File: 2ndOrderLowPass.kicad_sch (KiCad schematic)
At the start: 14 parts, among them U2 LM2904DR, U3 LM2904DR

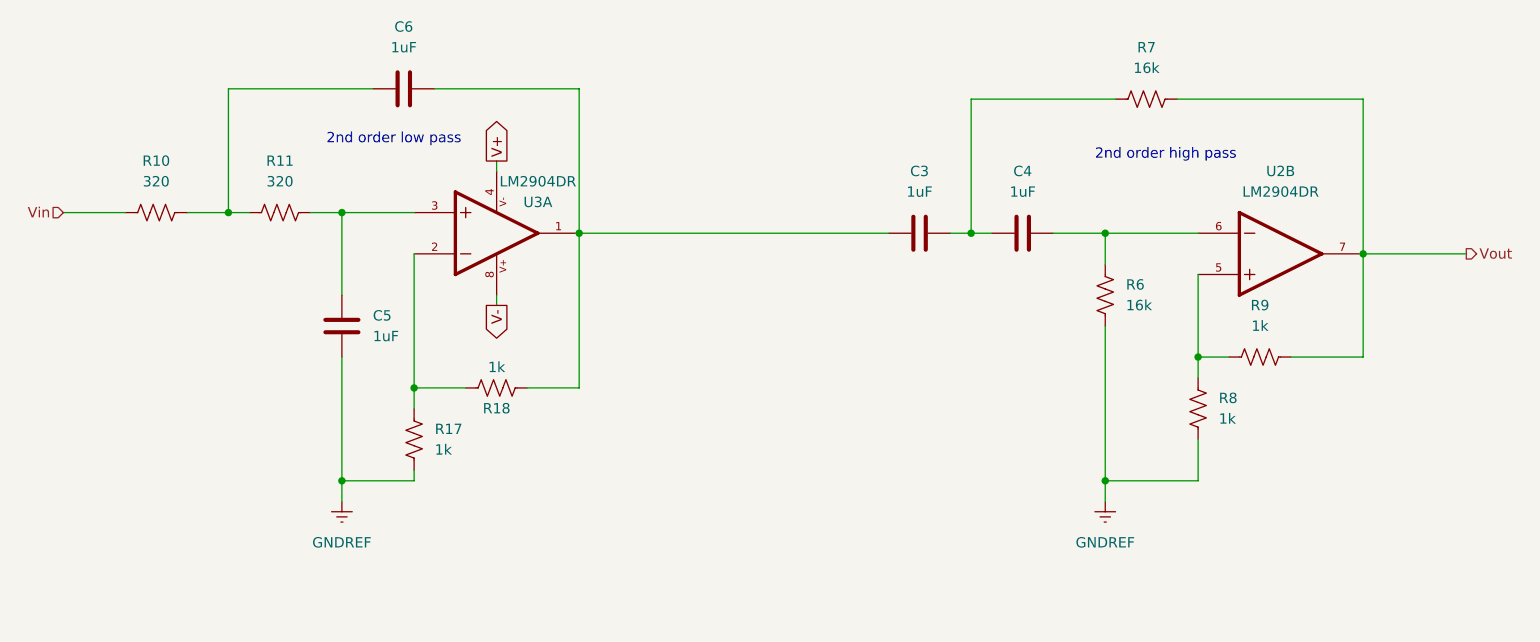
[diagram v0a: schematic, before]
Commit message: added new filter sims, and tweaked components for notch and bandpass filter and circuits for both as well
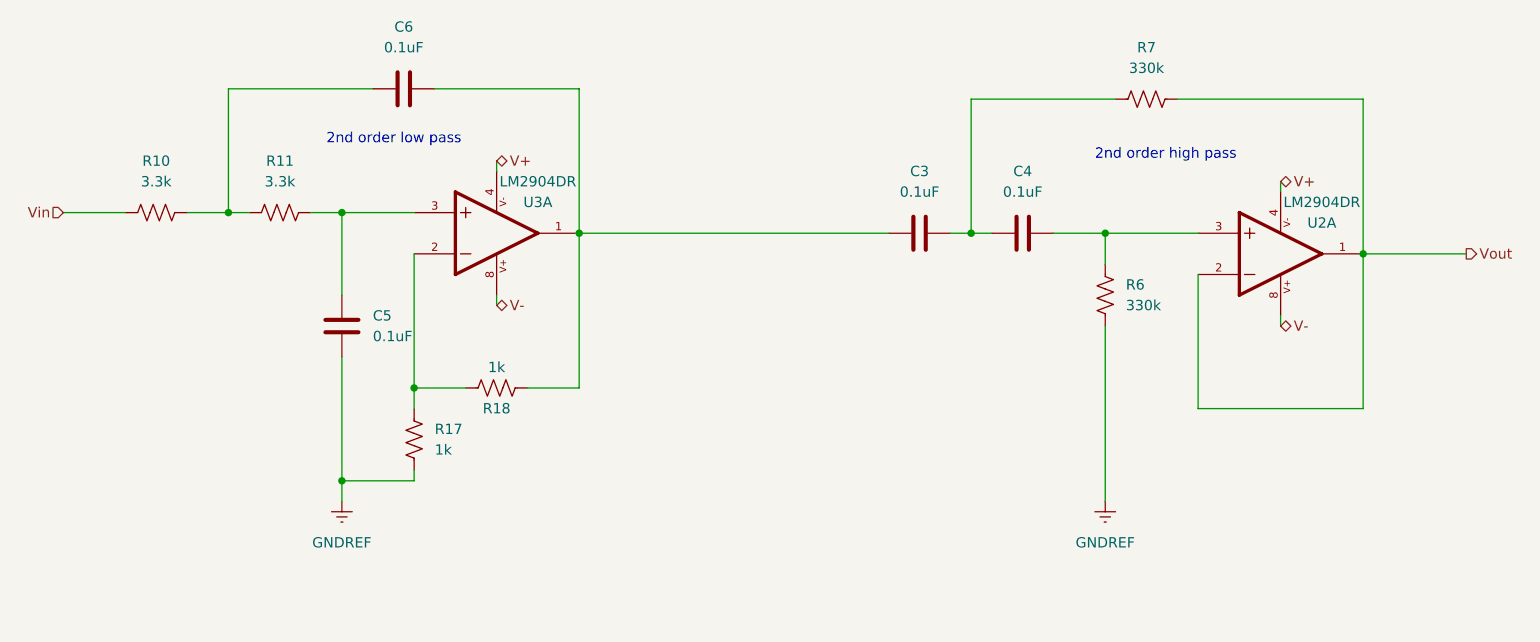
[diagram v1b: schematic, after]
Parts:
- removed R8, R9: 1k, symbol Device:R_US
- removed U2: LM2904DR, LM2904DR:SOIC127P599X175-8N, symbol Digikey2:LM2904DR
- added U2: LM2904DR, LM2904DR:SOIC127P599X175-8N, symbol Digikey2:LM2904DR
- C3, C4, C5, C6: value 1uF -> 0.1uF
- R10, R11: value 320 -> 3.3k
- R6, R7: value 16k -> 330k
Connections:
- net V+: now also U2.4
- net V-: now also U2.8
- net Vout: now also U2.1, U2.2
- net at C4.2, R6.1: now also U2.3

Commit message: swapped lpf and hpf in bandpass filter and added testpoints on various filter circuits
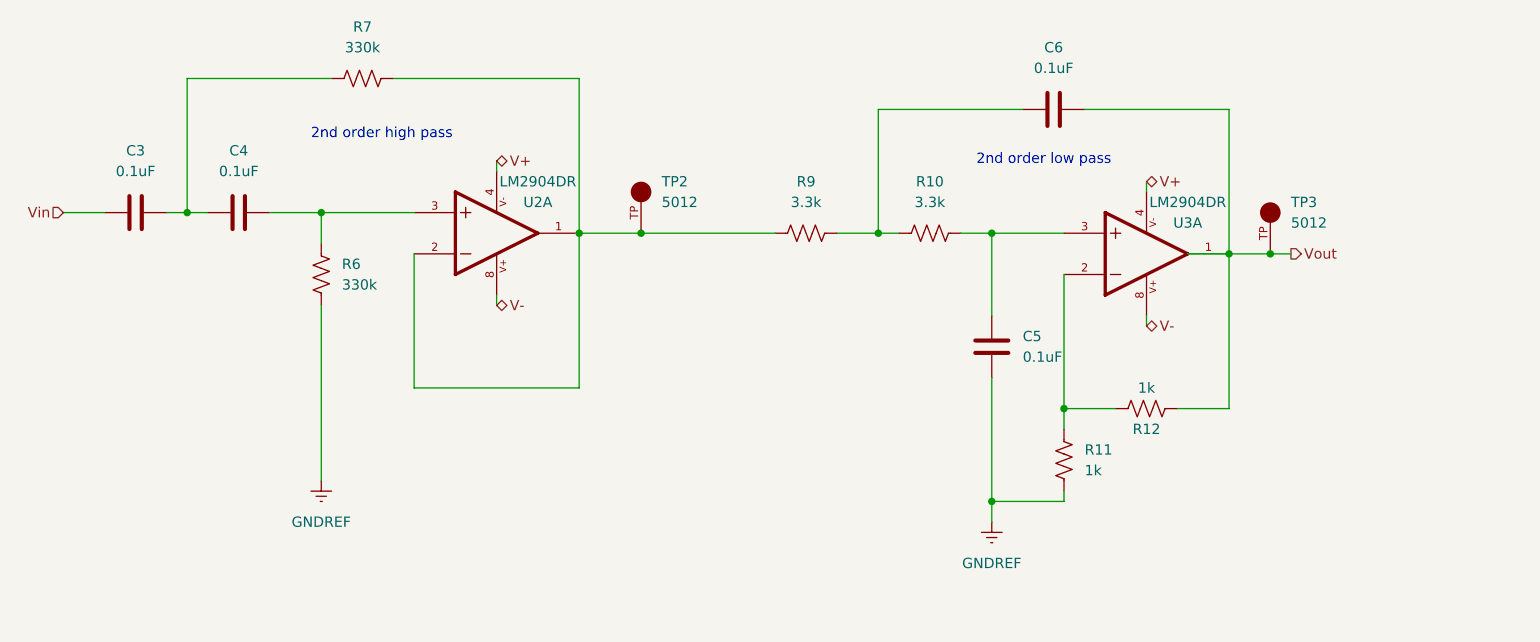
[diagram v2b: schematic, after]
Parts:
- removed R17, R18: 1k, symbol Device:R_US
- added R12: 1k, symbol Device:R_US
- added R9: 3.3k, symbol Device:R_US
- added TP2, TP3: 5012, 5012:TP_5012, symbol TP_5012:5012
- R11: value 3.3k -> 1k
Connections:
- net GNDREF: now also R11.2
- net Vin: now also C3.1; no longer R10.2
- net Vout: now also C6.2, U3.1, R12.2, TP3.TP; no longer R7.2, U2.1, U2.2
- net at U3.2: now also R11.1, R12.1
- net at C5.1, U3.3: now also R10.2; no longer R11.2
- net at C6.1, R10.1: now also R9.1; no longer R11.1
- new net: R7.2, R9.2, TP2.TP, U2.1, U2.2

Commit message: merge fix 2
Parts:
- removed U2, U3: LM2904DR, LM2904DR:SOIC127P599X175-8N, symbol Digikey2:LM2904DR
- added U5: LT1169CS8-PBF, SO-8_S_LIT, symbol symbols:LT1169CS8-PBF
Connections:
- net V+: now also U5.8 (V+)
- net V-: now also U5.4 (V-)
- net Vout: now also U5.7 (OUTB)
- net at R7.2, R9.2, TP2.TP: now also U5.1 (OUTA), U5.2 (-INA)
- net at R11.1, R12.1: now also U5.6 (-INB)
- net at C4.2, R6.1: now also U5.3 (+INA)
- net at C5.1, R10.2: now also U5.5 (+INB)
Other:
- moved on the sheet: C5, R11, R12

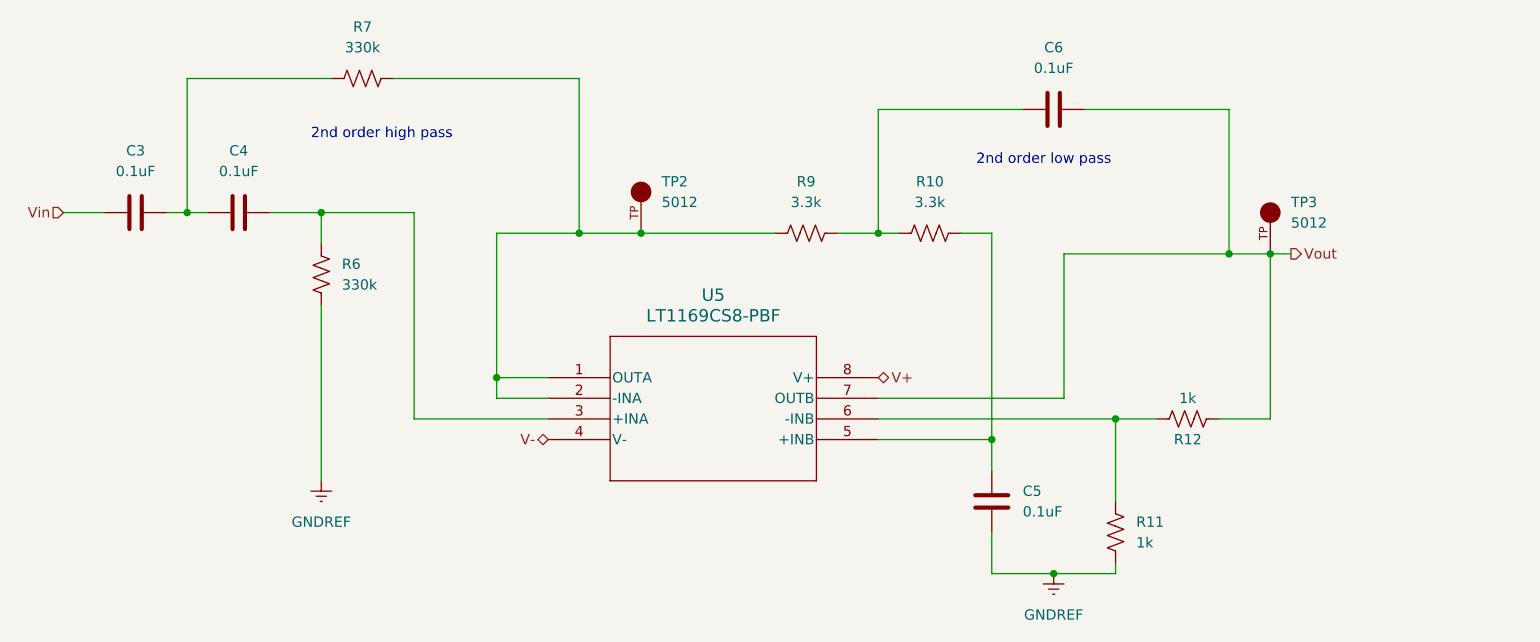
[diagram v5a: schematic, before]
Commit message: Reference Designator and Footprint Updates
Changed almost all reference designators to group similar components by what filter they are a part of and what value they have.

Need to:
- Sort symbol data for ADC and OpAmps to correct folders
- get footprint files for ADC and OpAmps
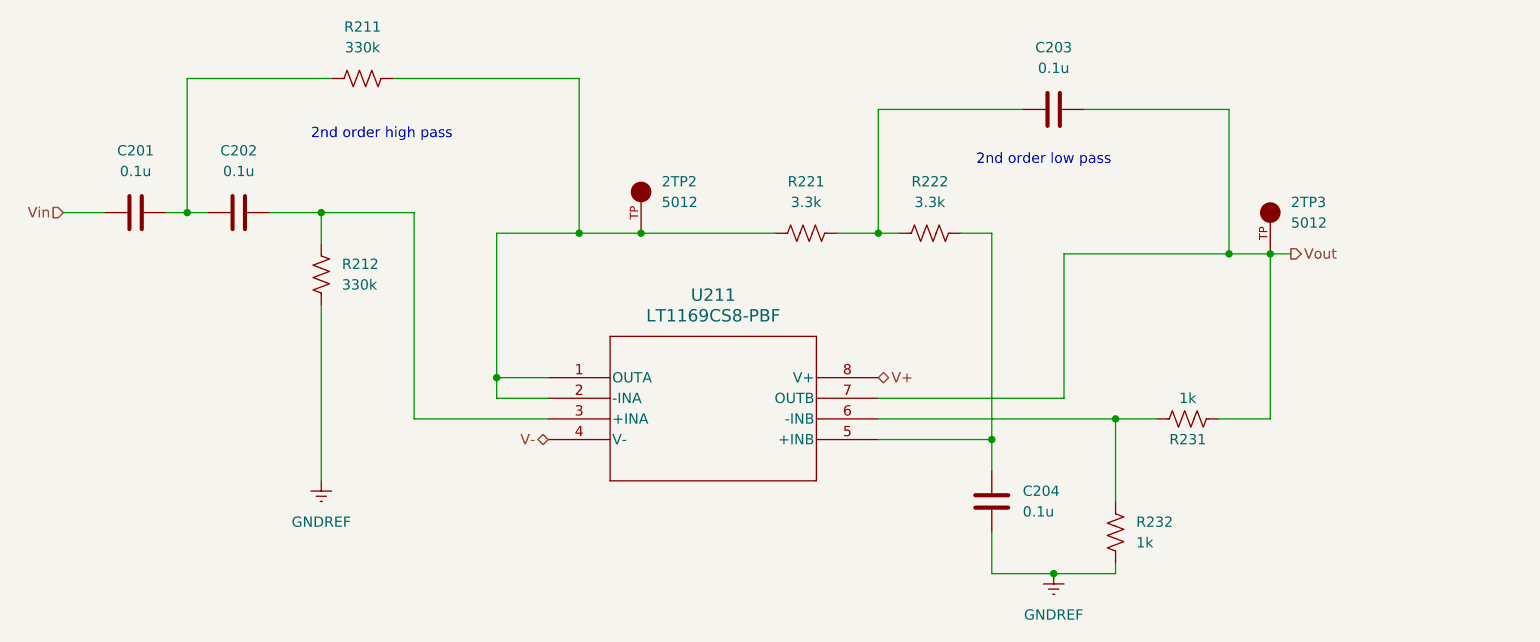
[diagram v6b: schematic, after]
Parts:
- 2TP2: renamed from TP2; footprint 5012:TP_5012 -> footprints:TP_5012
- 2TP3: renamed from TP3; footprint 5012:TP_5012 -> footprints:TP_5012
- C201: renamed from C3; value 0.1uF -> 0.1u; footprint (none) -> Capacitor_SMD:C_0603_1608Metric_Pad1.08x0.95mm_HandSolder
- C202: renamed from C4; value 0.1uF -> 0.1u; footprint (none) -> Capacitor_SMD:C_0603_1608Metric_Pad1.08x0.95mm_HandSolder
- C203: renamed from C6; value 0.1uF -> 0.1u; footprint (none) -> Capacitor_SMD:C_0603_1608Metric_Pad1.08x0.95mm_HandSolder
- C204: renamed from C5; value 0.1uF -> 0.1u; footprint (none) -> Capacitor_SMD:C_0603_1608Metric_Pad1.08x0.95mm_HandSolder
- R211: renamed from R7; footprint (none) -> Resistor_SMD:R_0603_1608Metric_Pad0.98x0.95mm_HandSolder
- R212: renamed from R6; footprint (none) -> Resistor_SMD:R_0603_1608Metric_Pad0.98x0.95mm_HandSolder
- R221: renamed from R9; footprint (none) -> Resistor_SMD:R_0603_1608Metric_Pad0.98x0.95mm_HandSolder
- R222: renamed from R10; footprint (none) -> Resistor_SMD:R_0603_1608Metric_Pad0.98x0.95mm_HandSolder
- R231: renamed from R12; footprint (none) -> Resistor_SMD:R_0603_1608Metric_Pad0.98x0.95mm_HandSolder
- R232: renamed from R11; footprint (none) -> Resistor_SMD:R_0603_1608Metric_Pad0.98x0.95mm_HandSolder
- U211: renamed from U5; footprint SO-8_S_LIT -> footprints:SOIC127P599X175-8N

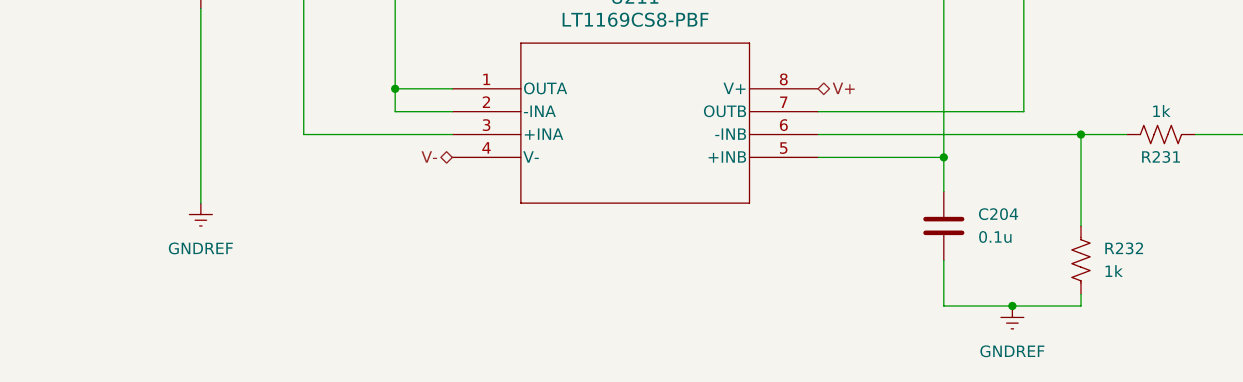
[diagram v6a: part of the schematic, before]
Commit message: updated GND symbols for appropriate seperatiion of analog and digital grounds
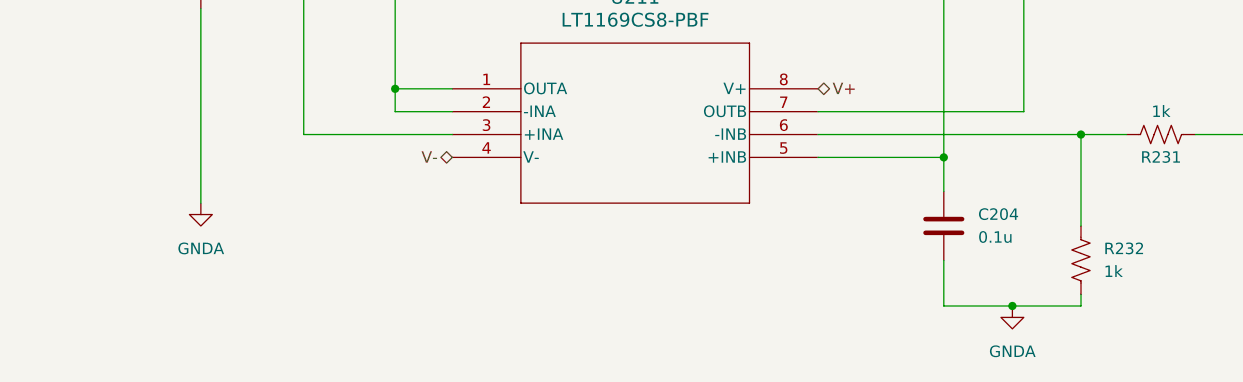
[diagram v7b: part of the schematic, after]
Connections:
- net GNDREF renamed GNDA
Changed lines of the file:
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@@
+    (stroke (width 0) (type default))
+  )
+  (wire (pts (xy 180.34 124.46) (xy 187.96 124.46))
     (stroke (width 0) (type default))
   )
@@
     (stroke (width 0) (type default))
   )
-  (wire (pts (xy 180.34 124.46) (xy 172.72 124.46))
+  (wire (pts (xy 172.72 124.46) (xy 180.34 124.46))
     (stroke (width 0) (type default))
   )
@@
   )
   (wire (pts (xy 168.91 82.55) (xy 172.72 82.55))
-    (stroke (width 0) (type default))
-  )
-  (wire (pts (xy 187.96 124.46) (xy 180.34 124.46))
     (stroke (width 0) (type default))
   )
@@
         (path "/c6167f6f-8a8c-40a1-9c06-7f0e8ea44639/fca8234f-eea0-4615-81d1-2ac2d4337d1e/3f67bfb0-bf5c-4aaf-9dac-9acb1a14cf3a"
           (reference "R431") (unit 1)
+        )
+      )
+    )
+  )
+  (symbol (lib_id "power:GNDA") (at 90.17 113.03 0) (unit 1)
+    (in_bom yes) (on_board yes) (dnp no) (fields_autoplaced)
+    (property "Reference" "#PWR05" (at 90.17 119.38 0)
+      (effects (font (size 1.27 1.27)) hide)
+    )
+    (property "Value" "GNDA" (at 90.17 118.11 0)
+      (effects (font (size 1.27 1.27)))
+    )
+    (property "Footprint" "" (at 90.17 113.03 0)
+      (effects (font (size 1.27 1.27)) hide)
+    )
+    (property "Datasheet" "" (at 90.17 113.03 0)
+      (effects (font (size 1.27 1.27)) hide)
+    )
+    (pin "1")
+    (instances
+      (project "TR_EMG"
+        (path "/c6167f6f-8a8c-40a1-9c06-7f0e8ea44639/a0268632-eb9a-430e-97ab-e20adbf6cd41/3f67bfb0-bf5c-4aaf-9dac-9acb1a14cf3a"
+          (reference "#PWR05") (unit 1)
+        )
+        (path "/c6167f6f-8a8c-40a1-9c06-7f0e8ea44639/e619882c-69e2-4357-9513-12f0ec23e799/3f67bfb0-bf5c-4aaf-9dac-9acb1a14cf3a"
+          (reference "#PWR06") (unit 1)
+        )
+        (path "/c6167f6f-8a8c-40a1-9c06-7f0e8ea44639/1e802adc-784c-4bfc-ac56-2ca34eafc640/3f67bfb0-bf5c-4aaf-9dac-9acb1a14cf3a"
+          (reference "#PWR07") (unit 1)
+        )
+        (path "/c6167f6f-8a8c-40a1-9c06-7f0e8ea44639/fca8234f-eea0-4615-81d1-2ac2d4337d1e/3f67bfb0-bf5c-4aaf-9dac-9acb1a14cf3a"
+          (reference "#PWR08") (unit 1)
         )
       )
@@
     )
   )
+  (symbol (lib_id "power:GNDA") (at 180.34 124.46 0) (unit 1)
+    (in_bom yes) (on_board yes) (dnp no) (fields_autoplaced)
+    (property "Reference" "#PWR01" (at 180.34 130.81 0)
+      (effects (font (size 1.27 1.27)) hide)
+    )
+    (property "Value" "GNDA" (at 180.34 129.54 0)
+      (effects (font (size 1.27 1.27)))
+    )
+    (property "Footprint" "" (at 180.34 124.46 0)
+      (effects (font (size 1.27 1.27)) hide)
+    )
+    (property "Datasheet" "" (at 180.34 124.46 0)
+      (effects (font (size 1.27 1.27)) hide)
+    )
+    (pin "1")
+    (instances
+      (project "TR_EMG"
+        (path "/c6167f6f-8a8c-40a1-9c06-7f0e8ea44639/a0268632-eb9a-430e-97ab-e20adbf6cd41/3f67bfb0-bf5c-4aaf-9dac-9acb1a14cf3a"
+          (reference "#PWR01") (unit 1)
+        )
+        (path "/c6167f6f-8a8c-40a1-9c06-7f0e8ea44639/e619882c-69e2-4357-9513-12f0ec23e799/3f67bfb0-bf5c-4aaf-9dac-9acb1a14cf3a"
+          (reference "#PWR03") (unit 1)
+        )
+        (path "/c6167f6f-8a8c-40a1-9c06-7f0e8ea44639/1e802adc-784c-4bfc-ac56-2ca34eafc640/3f67bfb0-bf5c-4aaf-9dac-9acb1a14cf3a"
+          (reference "#PWR09") (unit 1)
+        )
+        (path "/c6167f6f-8a8c-40a1-9c06-7f0e8ea44639/fca8234f-eea0-4615-81d1-2ac2d4337d1e/3f67bfb0-bf5c-4aaf-9dac-9acb1a14cf3a"
+          (reference "#PWR010") (unit 1)
+        )
+      )
+    )
+  )
   (symbol (lib_id "Device:C") (at 172.72 115.57 0) (unit 1)
     (in_bom yes) (on_board yes) (dnp no) (fields_autoplaced)
@@
     )
   )
-  (symbol (lib_id "power:GNDREF") (at 90.17 113.03 0) (unit 1)
-    (in_bom yes) (on_board yes) (dnp no) (fields_autoplaced)
-    (property "Reference" "#PWR0102" (at 90.17 119.38 0)
-      (effects (font (size 1.27 1.27)) hide)
-    )
-    (property "Value" "GNDREF" (at 90.17 118.11 0)
-      (effects (font (size 1.27 1.27)))
-    )
-    (property "Footprint" "" (at 90.17 113.03 0)
-      (effects (font (size 1.27 1.27)) hide)
-    )
-    (property "Datasheet" "" (at 90.17 113.03 0)
-      (effects (font (size 1.27 1.27)) hide)
-    )
-    (pin "1")
-    (instances
-      (project "TR_EMG"
-        (path "/c6167f6f-8a8c-40a1-9c06-7f0e8ea44639/e619882c-69e2-4357-9513-12f0ec23e799/3f67bfb0-bf5c-4aaf-9dac-9acb1a14cf3a"
-          (reference "#PWR0102") (unit 1)
-        )
-        (path "/c6167f6f-8a8c-40a1-9c06-7f0e8ea44639/a0268632-eb9a-430e-97ab-e20adbf6cd41/3f67bfb0-bf5c-4aaf-9dac-9acb1a14cf3a"
-          (reference "#PWR01") (unit 1)
-        )
-        (path "/c6167f6f-8a8c-40a1-9c06-7f0e8ea44639/1e802adc-784c-4bfc-ac56-2ca34eafc640/3f67bfb0-bf5c-4aaf-9dac-9acb1a14cf3a"
-          (reference "#PWR0105") (unit 1)
-        )
-        (path "/c6167f6f-8a8c-40a1-9c06-7f0e8ea44639/fca8234f-eea0-4615-81d1-2ac2d4337d1e/3f67bfb0-bf5c-4aaf-9dac-9acb1a14cf3a"
-          (reference "#PWR0108") (unit 1)
-        )
-      )
-    )
-  )
   (symbol (lib_id "Device:R_US") (at 187.96 119.38 0) (unit 1)
     (in_bom yes) (on_board yes) (dnp no) (fields_autoplaced)
@@
         )
       )
-    )
-  )
-  (symbol (lib_id "power:GNDREF") (at 180.34 124.46 0) (unit 1)
-    (in_bom yes) (on_board yes) (dnp no) (fields_autoplaced)
-    (property "Reference" "#PWR0101" (at 180.34 130.81 0)
-      (effects (font (size 1.27 1.27)) hide)
-    )
-    (property "Value" "GNDREF" (at 180.34 129.54 0)
-      (effects (font (size 1.27 1.27)))
-    )
-    (property "Footprint" "" (at 180.34 124.46 0)
-      (effects (font (size 1.27 1.27)) hide)
-    )
-    (property "Datasheet" "" (at 180.34 124.46 0)
-      (effects (font (size 1.27 1.27)) hide)
-    )
-    (pin "1")
-    (instances
-      (project "TR_EMG"
-        (path "/c6167f6f-8a8c-40a1-9c06-7f0e8ea44639/e619882c-69e2-4357-9513-12f0ec23e799/3f67bfb0-bf5c-4aaf-9dac-9acb1a14cf3a"
-          (reference "#PWR0101") (unit 1)
-        )
-        (path "/c6167f6f-8a8c-40a1-9c06-7f0e8ea44639/a0268632-eb9a-430e-97ab-e20adbf6cd41/3f67bfb0-bf5c-4aaf-9dac-9acb1a14cf3a"
-          (reference "#PWR03") (unit 1)
-        )
-        (path "/c6167f6f-8a8c-40a1-9c06-7f0e8ea44639/1e802adc-784c-4bfc-ac56-2ca34eafc640/3f67bfb0-bf5c-4aaf-9dac-9acb1a14cf3a"
-          (reference "#PWR0104") (unit 1)
-        )
-        (path "/c6167f6f-8a8c-40a1-9c06-7f0e8ea44639/fca8234f-eea0-4615-81d1-2ac2d4337d1e/3f67bfb0-bf5c-4aaf-9dac-9acb1a14cf3a"
-          (reference "#PWR0107") (unit 1)
-        )
-      )

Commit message: renamed and relinked footprints with better clarity footprint file names
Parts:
- U211: footprint footprints:SOIC127P599X175-8N -> footprints:LT-SOIC127P599X175-8N
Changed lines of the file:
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@@
       (effects (font (size 1.524 1.524)))
     )
-    (property "Footprint" "footprints:SOIC127P599X175-8N" (at 118.11 100.33 0)
+    (property "Footprint" "footprints:LT-SOIC127P599X175-8N" (at 118.11 100.33 0)
       (effects (font (size 1.27 1.27) italic) hide)
     )
